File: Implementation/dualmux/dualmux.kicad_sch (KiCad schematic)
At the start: 3 parts, among them U1 74HC00

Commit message: Progress on designing card layout
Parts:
- A1: footprint (none) -> Connector_Nandy:EDAC_395-DualMux-CardEdge
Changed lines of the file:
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@@
     (pin "2")
     (instances
-      (project "mux9"
+      (project "dualmux"
         (path "/ecd0978f-53c1-4da1-845e-40c294143218"
           (reference "U1") (unit 4)
@@
     (pin "2")
     (instances
-      (project "mux9"
+      (project "dualmux"
         (path "/ecd0978f-53c1-4da1-845e-40c294143218"
           (reference "U1") (unit 5)
@@
     (pin "1")
     (instances
-      (project "mux9"
+      (project "dualmux"
         (path "/ecd0978f-53c1-4da1-845e-40c294143218"
           (reference "#PWR04") (unit 1)
@@
     (pin "2")
     (instances
-      (project "mux9"
+      (project "dualmux"
         (path "/ecd0978f-53c1-4da1-845e-40c294143218"
           (reference "C1") (unit 1)
@@
     (pin "2")
     (instances
-      (project "mux9"
+      (project "dualmux"
         (path "/ecd0978f-53c1-4da1-845e-40c294143218"
           (reference "U1") (unit 3)
@@
     (pin "1")
     (instances
-      (project "mux9"
+      (project "dualmux"
         (path "/ecd0978f-53c1-4da1-845e-40c294143218"
           (reference "#PWR03") (unit 1)
@@
     (pin "1")
     (instances
-      (project "mux9"
+      (project "dualmux"
         (path "/ecd0978f-53c1-4da1-845e-40c294143218"
           (reference "#PWR031") (unit 1)
@@
     (pin "2")
     (instances
-      (project "mux9"
+      (project "dualmux"
         (path "/ecd0978f-53c1-4da1-845e-40c294143218"
           (reference "U1") (unit 2)
@@
     (pin "2")
     (instances
-      (project "mux9"
+      (project "dualmux"
         (path "/ecd0978f-53c1-4da1-845e-40c294143218"
           (reference "U1") (unit 1)
@@
     (pin "1")
     (instances
-      (project "mux9"
+      (project "dualmux"
         (path "/ecd0978f-53c1-4da1-845e-40c294143218"
           (reference "#PWR01") (unit 1)
@@
     (pin "1")
     (instances
-      (project "mux9"
+      (project "dualmux"
         (path "/ecd0978f-53c1-4da1-845e-40c294143218"
           (reference "#PWR032") (unit 1)
@@
       (effects (font (size 1.27 1.27)))
     )
-    (property "Footprint" "" (at 52.07 128.27 0)
+    (property "Footprint" "Connector_Nandy:EDAC_395-DualMux-CardEdge" (at 52.07 128.27 0)
       (effects (font (size 1.27 1.27)) hide)
     )
@@
     (pin "1")
     (instances
-      (project "mux9"
+      (project "dualmux"
         (path "/ecd0978f-53c1-4da1-845e-40c294143218"
           (reference "A1") (unit 3)
@@
     (pin "1")
     (instances
-      (project "mux9"
+      (project "dualmux"
         (path "/ecd0978f-53c1-4da1-845e-40c294143218"
           (reference "#PWR06") (unit 1)
@@
       (effects (font (size 1.27 1.27)))
     )
-    (property "Footprint" "" (at 215.9 113.03 0)
+    (property "Footprint" "Connector_Nandy:EDAC_395-DualMux-CardEdge" (at 215.9 113.03 0)
       (effects (font (size 1.27 1.27)) hide)
     )
@@
     (pin "1")
     (instances
-      (project "mux9"
+      (project "dualmux"
         (path "/ecd0978f-53c1-4da1-845e-40c294143218"
           (reference "A1") (unit 2)
@@
     (pin "1")
     (instances
-      (project "mux9"
+      (project "dualmux"
         (path "/ecd0978f-53c1-4da1-845e-40c294143218"
           (reference "#PWR05") (unit 1)
@@
       (effects (font (size 1.27 1.27)))
     )
-    (property "Footprint" "" (at 215.9 54.61 0)
+    (property "Footprint" "Connector_Nandy:EDAC_395-DualMux-CardEdge" (at 215.9 54.61 0)
       (effects (font (size 1.27 1.27)) hide)
     )
@@
     (pin "1")
     (instances
-      (project "mux9"
+      (project "dualmux"
         (path "/ecd0978f-53c1-4da1-845e-40c294143218"
           (reference "A1") (unit 1)
@@
     (pin "1")
     (instances
-      (project "mux9"
+      (project "dualmux"
         (path "/ecd0978f-53c1-4da1-845e-40c294143218"
           (reference "#PWR02") (unit 1)
@@
     )
     (instances
-      (project "mux9"
+      (project "dualmux"
         (path "/ecd0978f-53c1-4da1-845e-40c294143218" (page "3"))
       )
@@
     )
     (instances
-      (project "mux9"
+      (project "dualmux"
         (path "/ecd0978f-53c1-4da1-845e-40c294143218" (page "5"))
       )
@@
     )
     (instances
-      (project "mux9"
+      (project "dualmux"
         (path "/ecd0978f-53c1-4da1-845e-40c294143218" (page "4"))
       )
@@
     )
     (instances
-      (project "mux9"
+      (project "dualmux"
         (path "/ecd0978f-53c1-4da1-845e-40c294143218" (page "2"))
       )
@@
     )
     (instances
-      (project "mux9"
+      (project "dualmux"
         (path "/ecd0978f-53c1-4da1-845e-40c294143218" (page "8"))
       )
@@
     )
     (instances
-      (project "mux9"
+      (project "dualmux"
         (path "/ecd0978f-53c1-4da1-845e-40c294143218" (page "6"))
       )
@@
     )
     (instances
-      (project "mux9"
+      (project "dualmux"
         (path "/ecd0978f-53c1-4da1-845e-40c294143218" (page "9"))
       )
@@
     )
     (instances
-      (project "mux9"
+      (project "dualmux"
         (path "/ecd0978f-53c1-4da1-845e-40c294143218" (page "7"))
       )

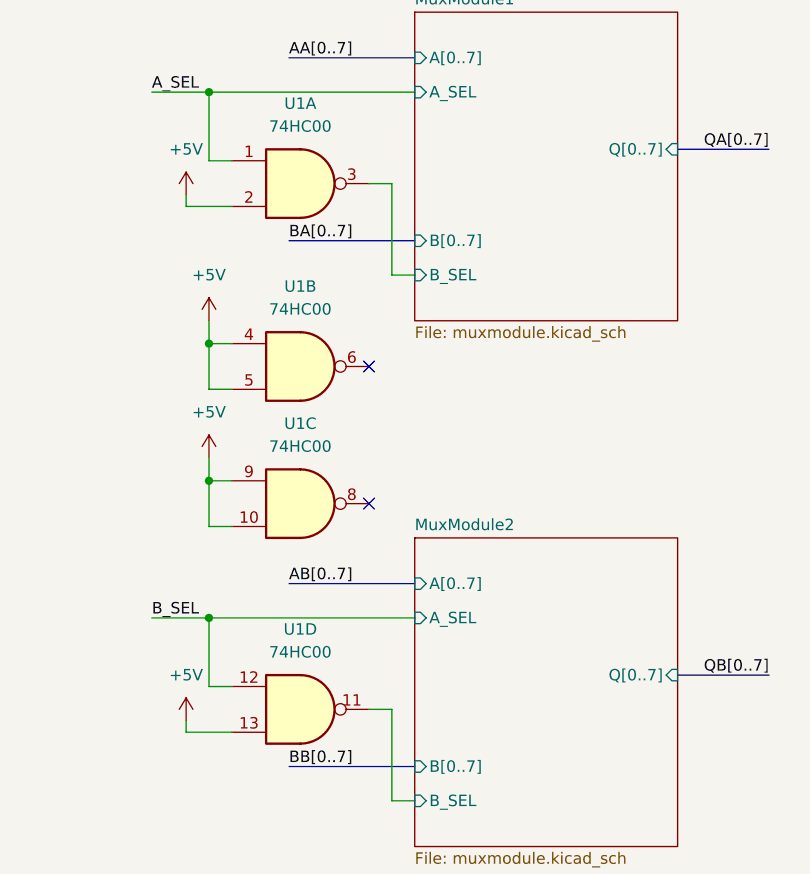
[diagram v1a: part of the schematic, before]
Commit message: Some of the routing done, need to figure out how to get everything to the connector
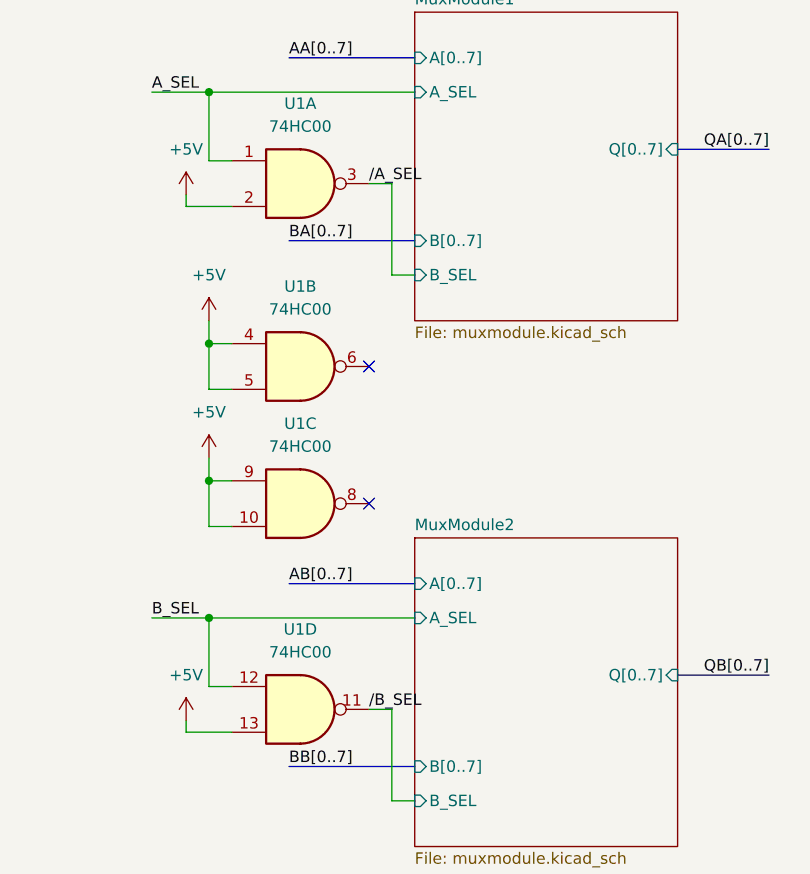
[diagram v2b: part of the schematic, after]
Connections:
- net MuxModule1/B_SEL renamed /A_SEL
- net MuxModule2/B_SEL renamed /B_SEL
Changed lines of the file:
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@@
+    (effects (font (size 1.27 1.27)) (justify left bottom))
+  )
+  (label "{slash}A_SEL" (at 115.57 59.69 0) (fields_autoplaced)
     (effects (font (size 1.27 1.27)) (justify left bottom))
   )
@@
     (effects (font (size 1.27 1.27)) (justify left bottom))
   )
+  (label "{slash}B_SEL" (at 115.57 118.11 0) (fields_autoplaced)
+    (effects (font (size 1.27 1.27)) (justify left bottom))
+  )

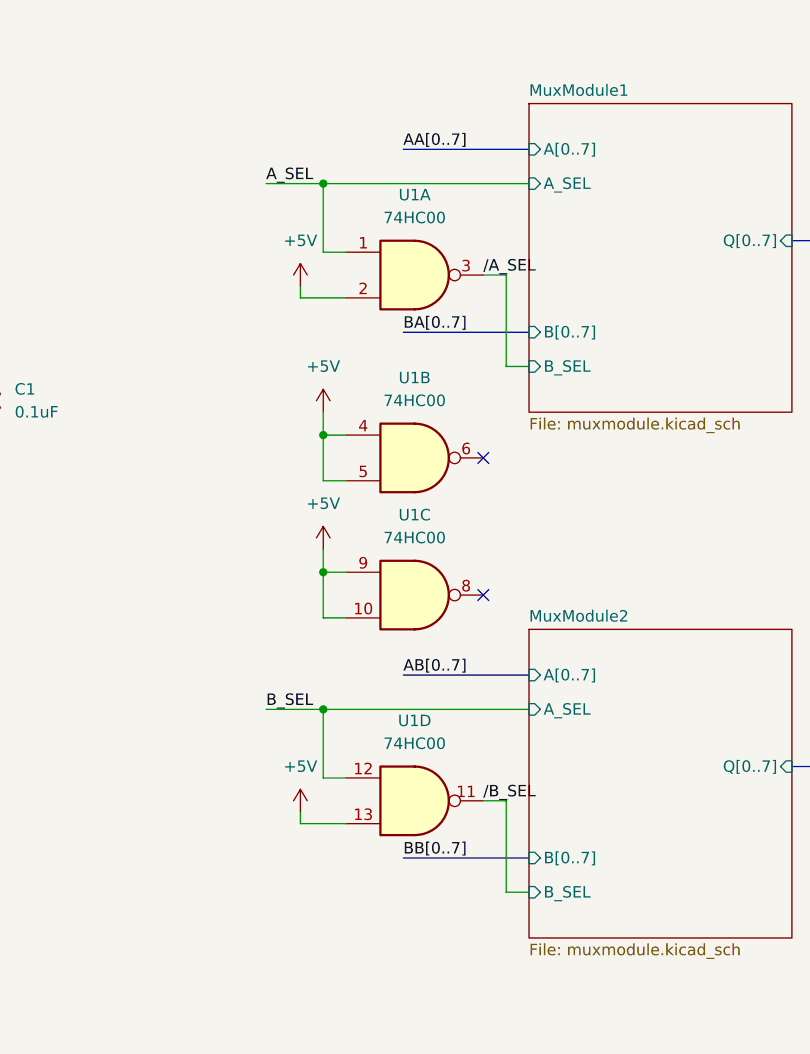
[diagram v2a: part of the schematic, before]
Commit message: Most of mux routing
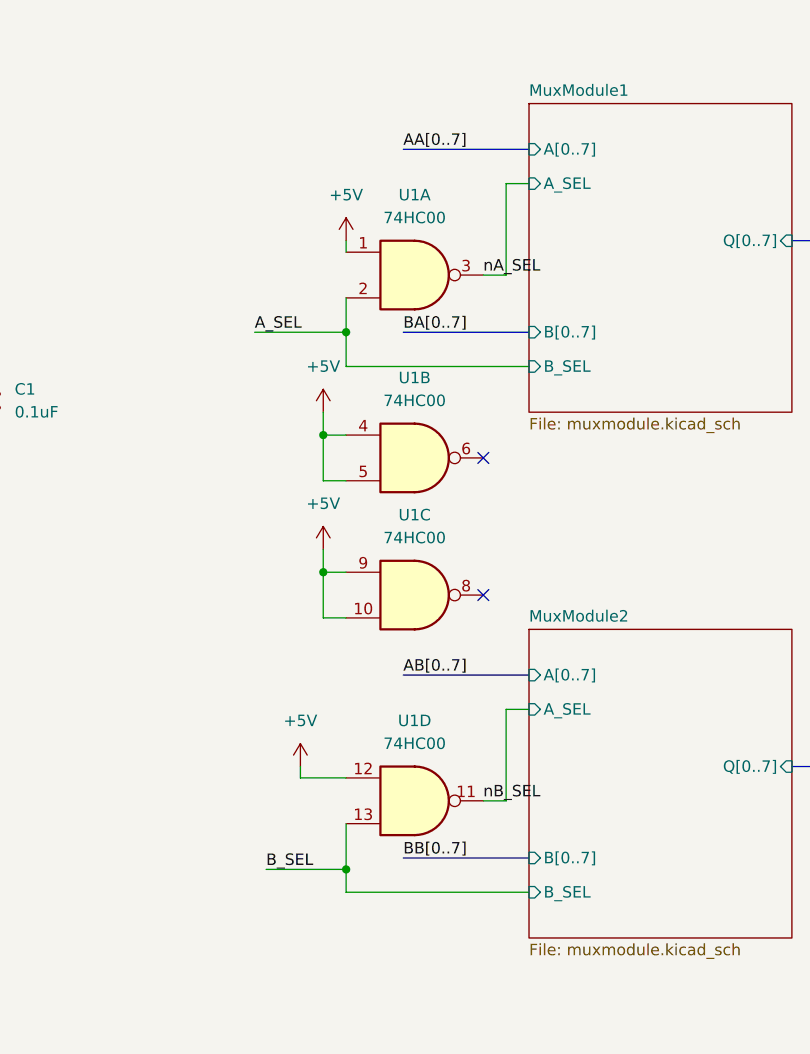
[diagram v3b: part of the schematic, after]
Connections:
- net +5V: now also U1.1, U1.12; no longer U1.13, U1.2
- net A_SEL: now also U1.2; no longer U1.1
- net B_SEL: now also U1.13; no longer U1.12
- net /A_SEL renamed nA_SEL
- net /B_SEL renamed nB_SEL
